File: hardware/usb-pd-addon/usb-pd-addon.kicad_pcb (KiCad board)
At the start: 4 copper layers, 48 x 40 mm, 75 parts, among them J1 Conn_02x10_Odd_Even, J11 Conn_02x02, J2 Conn_02x10_Odd_Even, J3 USB_TYPE_C, J4 USB_TYPE_C, J6 TPAS, J7 TPBS, J8 Conn_02x03_Odd_Even, J9 Conn_02x02, U1 FUSB302B, U10 NC7SB3157P6X, U11 NC7SB3157P6X, U2 AP2171W, U3 SN74AVC1T45DCKR, U4 SN74AVC1T45DCKR, U5 SN74AVC1T45DCKR, U6 SN74AVC1T45DBVR, U7 AP2127K-ADJ, U8 NC7SB3157P6X, U9 NC7SB3157P6X

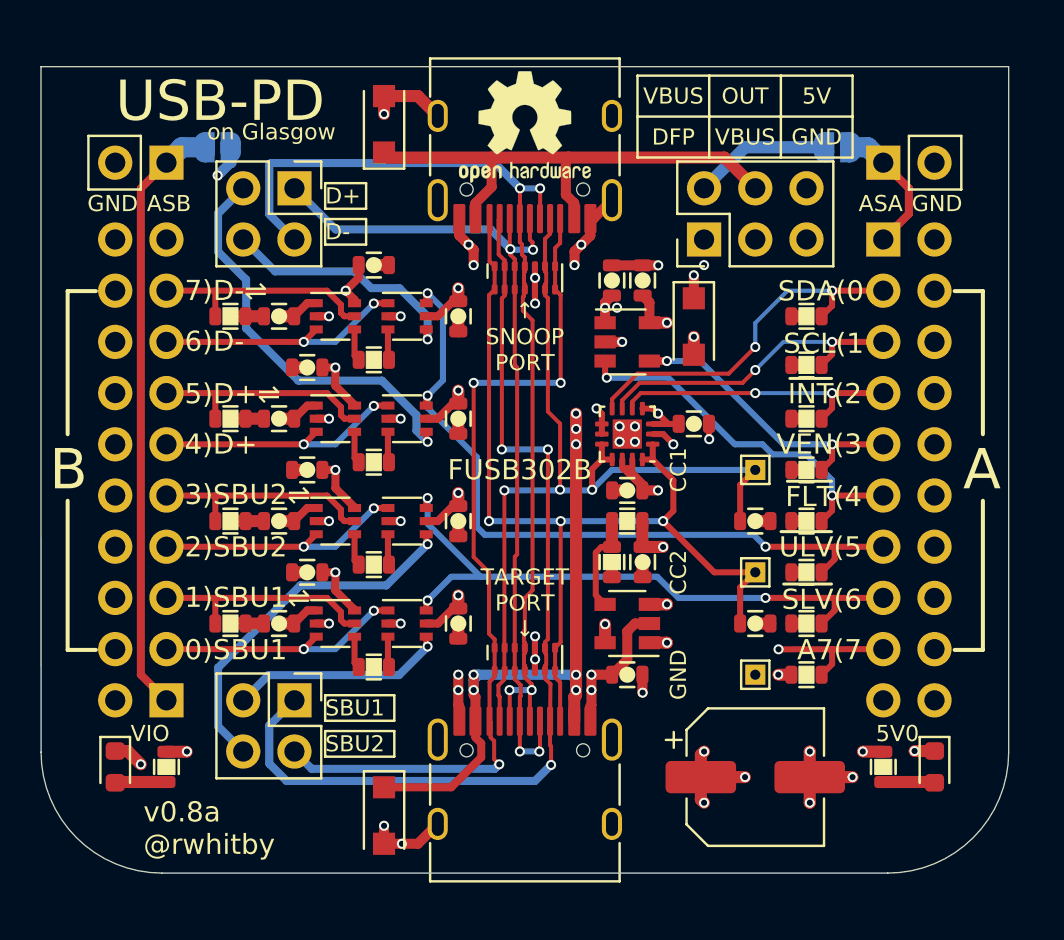
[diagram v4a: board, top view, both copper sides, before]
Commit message: Small silk improvements
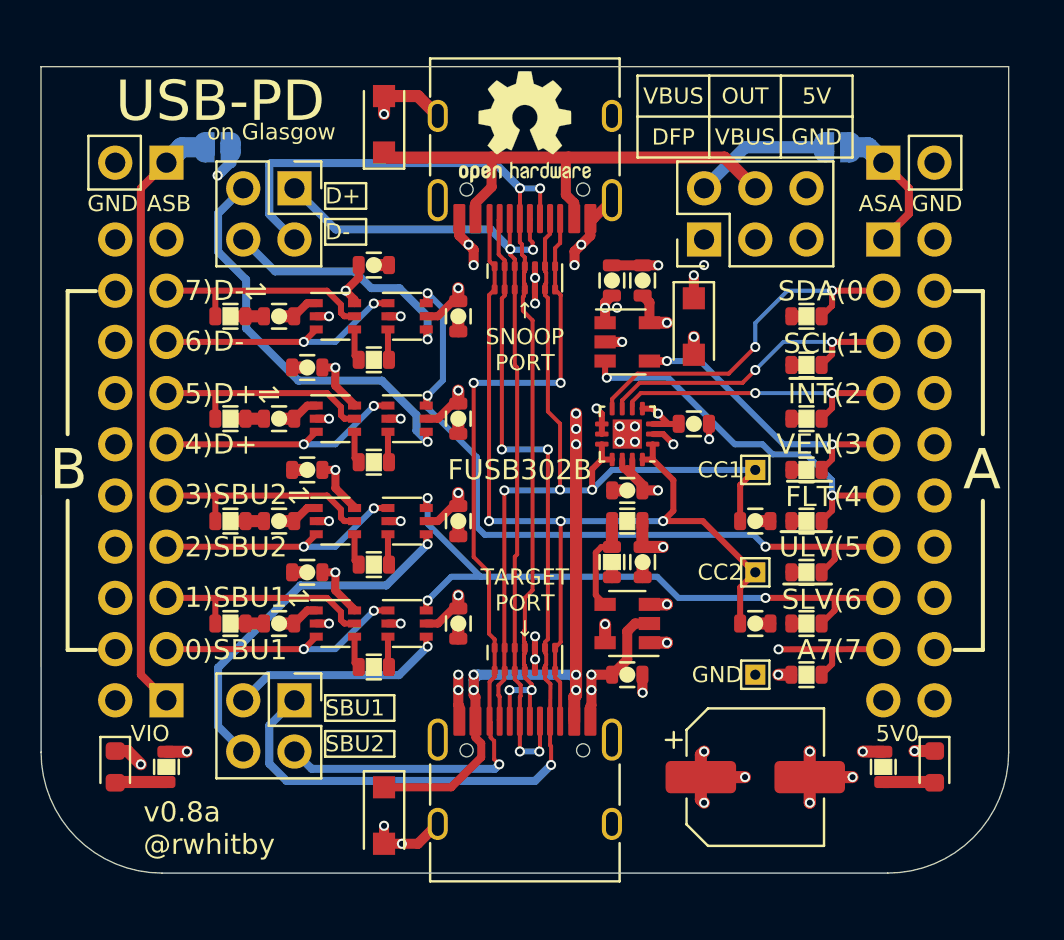
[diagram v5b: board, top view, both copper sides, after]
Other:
- board text added: "⇌D+(5"
- board text added: "⇌D-(7"
- board text added: "⇌SBU1(1"
- board text added: "⇌SBU2(3"
- board text removed: "D+⇌(5"
- board text removed: "D-⇌(7"
- board text removed: "SBU1⇌(1"
- board text removed: "SBU2⇌(3"
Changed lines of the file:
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@@
   )
   (setup
-    (last_trace_width 1)
+    (last_trace_width 0.2)
     (user_trace_width 0.3)
     (user_trace_width 0.4)
@@
       (effects (font (size 1 1) (thickness 0.15)))
     )
-    (fp_text user %R (at 1.27 1.27) (layer F.Fab)
-      (effects (font (size 1 1) (thickness 0.15)))
-    )
     (fp_line (start 0 -1.27) (end 3.81 -1.27) (layer F.Fab) (width 0.1))
     (fp_line (start 3.81 -1.27) (end 3.81 3.81) (layer F.Fab) (width 0.1))
@@
     (fp_line (start 4.35 4.35) (end 4.35 -1.8) (layer F.CrtYd) (width 0.05))
     (fp_line (start 4.35 -1.8) (end -1.8 -1.8) (layer F.CrtYd) (width 0.05))
+    (fp_text user %R (at 1.27 1.27) (layer F.Fab)
+      (effects (font (size 1 1) (thickness 0.15)))
+    )
     (pad 4 thru_hole oval (at 2.54 2.54 270) (size 1.7 1.7) (drill 1) (layers *.Cu *.Mask)
       (net 50 "Net-(J11-Pad4)"))
@@
       (effects (font (size 1 1) (thickness 0.15)))
     )
-    (fp_text user %R (at 1.27 1.27) (layer F.Fab)
-      (effects (font (size 1 1) (thickness 0.15)))
-    )
     (fp_line (start 0 -1.27) (end 3.81 -1.27) (layer F.Fab) (width 0.1))
     (fp_line (start 3.81 -1.27) (end 3.81 3.81) (layer F.Fab) (width 0.1))
@@
     (fp_line (start 4.35 4.35) (end 4.35 -1.8) (layer F.CrtYd) (width 0.05))
     (fp_line (start 4.35 -1.8) (end -1.8 -1.8) (layer F.CrtYd) (width 0.05))
+    (fp_text user %R (at 1.27 1.27) (layer F.Fab)
+      (effects (font (size 1 1) (thickness 0.15)))
+    )
     (pad 4 thru_hole oval (at 2.54 2.54 270) (size 1.7 1.7) (drill 1) (layers *.Cu *.Mask)
       (net 48 "Net-(J9-Pad4)"))
@@
   )
   (gr_poly (pts (xy 61.595 50.90795) (xy 60.325 50.90795) (xy 60.325 49.67605) (xy 61.595 49.67605)) (layer B.Mask) (width 0.1))
-  (gr_text GND (at 63.5 62.23 90) (layer F.SilkS)
-    (effects (font (size 0.8 0.8) (thickness 0.15)))
+  (gr_text GND (at 66.675 62.23) (layer F.SilkS)
+    (effects (font (size 0.8 0.8) (thickness 0.15)) (justify right))
   )
-  (gr_text CC1 (at 63.5 52.07 90) (layer F.SilkS)
-    (effects (font (size 0.8 0.8) (thickness 0.15)))
+  (gr_text CC1 (at 66.675 52.07) (layer F.SilkS)
+    (effects (font (size 0.8 0.8) (thickness 0.15)) (justify right))
   )
-  (gr_text CC2 (at 63.5 57.15 90) (layer F.SilkS)
-    (effects (font (size 0.8 0.8) (thickness 0.15)))
+  (gr_text CC2 (at 66.675 57.15) (layer F.SilkS)
+    (effects (font (size 0.8 0.8) (thickness 0.15)) (justify right))
   )
   (gr_text JLCJLCJLCJLC (at 55.88 71.3105) (layer B.SilkS)
     (effects (font (size 0.8 0.8) (thickness 0.15)) (justify mirror))
   )
-  (gr_text "D-⇌(7" (at 39.5 43.25) (layer B.SilkS)
+  (gr_text "⇌D-(7" (at 39.5 43.25) (layer B.SilkS)
     (effects (font (size 1 1) (thickness 0.15)) (justify right mirror))
   )
@@
     (effects (font (size 1 1) (thickness 0.15)) (justify right mirror))
   )
-  (gr_text "SBU1⇌(1" (at 39.45 58.4) (layer B.SilkS)
+  (gr_text "⇌SBU1(1" (at 39.45 58.4) (layer B.SilkS)
     (effects (font (size 1 1) (thickness 0.15)) (justify right mirror))
   )
@@
     (effects (font (size 1 1) (thickness 0.15)) (justify right mirror))
   )
-  (gr_text "SBU2⇌(3" (at 39.45 53.3) (layer B.SilkS)
+  (gr_text "⇌SBU2(3" (at 39.45 53.3) (layer B.SilkS)
     (effects (font (size 1 1) (thickness 0.15)) (justify right mirror))
   )
@@
     (effects (font (size 1 1) (thickness 0.15)) (justify right mirror))
   )
-  (gr_text "D+⇌(5" (at 39.45 48.3) (layer B.SilkS)
+  (gr_text "⇌D+(5" (at 39.45 48.3) (layer B.SilkS)
     (effects (font (size 1 1) (thickness 0.15)) (justify right mirror))
   )
@@
   (via (at 49.7205 59.69) (size 0.5) (drill 0.3) (layers F.Cu B.Cu) (net 1))
   (segment (start 49.088 59.69) (end 49.7205 59.69) (width 0.4) (layer F.Cu) (net 1) (status 10))
-  (via (at 44.912 60.96) (size 0.5) (drill 0.3) (layers F.Cu B.Cu) (net 17))
   (segment (start 45.532 59.69) (end 46.1645 59.69) (width 0.4) (layer F.Cu) (net 1) (status 10))
   (via (at 46.1645 59.69) (size 0.5) (drill 0.3) (layers F.Cu B.Cu) (net 1))
@@
   (segment (start 62.2225 50.792) (end 62.2225 51.5545) (width 0.3) (layer F.Cu) (net 7) (status 10))
   (segment (start 61.71 51.5545) (end 62.2225 51.5545) (width 0.3) (layer F.Cu) (net 7) (status 10))
-  (segment (start 65.278 57.15) (end 67.31 57.15) (width 0.3) (layer F.Cu) (net 7))
-  (segment (start 62.738 54.61) (end 65.278 57.15) (width 0.3) (layer F.Cu) (net 7))
   (segment (start 66.56 57.9) (end 66.56 59.69) (width 0.3) (layer F.Cu) (net 7))
   (segment (start 67.31 57.15) (end 66.56 57.9) (width 0.3) (layer F.Cu) (net 7))
+  (segment (start 67.2465 57.15) (end 67.31 57.15) (width 0.3) (layer F.Cu) (net 7))
+  (segment (start 64.7065 54.61) (end 67.2465 57.15) (width 0.3) (layer F.Cu) (net 7))
+  (segment (start 62.738 54.61) (end 64.7065 54.61) (width 0.3) (layer F.Cu) (net 7))
   (segment (start 54.63 64.535) (end 54.58001 64.48501) (width 0.2) (layer F.Cu) (net 8) (status 30))
   (segment (start 57.13 40.360346) (end 57.13 39.605) (width 0.2) (layer F.Cu) (net 8) (status 20))
@@
   (segment (start 62.2225 50.292) (end 62.738 50.292) (width 0.3) (layer F.Cu) (net 11) (status 10))
   (segment (start 62.738 50.292) (end 63.246 50.8) (width 0.3) (layer F.Cu) (net 11))
-  (segment (start 67.31 40.386) (end 67.31 40.64) (width 0.5) (layer B.Cu) (net 11) (status 30))
-  (segment (start 65.024 38.1) (end 67.31 40.386) (width 0.6) (layer In2.Cu) (net 11) (status 30))
-  (segment (start 64.77 38.1) (end 65.024 38.1) (width 0.5) (layer B.Cu) (net 11) (status 30))
   (segment (start 53.34 62.992) (end 53.34 62.23) (width 0.5) (layer F.Cu) (net 11))
   (segment (start 53.34 62.484) (end 53.594 62.23) (width 0.5) (layer B.Cu) (net 11))
@@
   (segment (start 53.43 65.346998) (end 53.715001 65.631999) (width 0.4) (layer F.Cu) (net 11))
   (segment (start 53.43 64.535) (end 53.43 65.346998) (width 0.4) (layer F.Cu) (net 11))
+  (segment (start 67.31 40.399998) (end 67.31 40.64) (width 0.8) (layer In2.Cu) (net 11))
+  (segment (start 65.010002 38.1) (end 67.31 40.399998) (width 0.8) (layer In2.Cu) (net 11))
+  (segment (start 64.77 38.1) (end 65.010002 38.1) (width 0.8) (layer In2.Cu) (net 11))
   (segment (start 57.38 41.0652) (end 57.63 40.8152) (width 0.2) (layer F.Cu) (net 12))
   (segment (start 57.38 41.97) (end 57.38 41.0652) (width 0.2) (layer F.Cu) (net 12) (status 10))
@@
   (segment (start 52.578 53.213) (end 53.328001 52.462999) (width 0.6) (layer In2.Cu) (net 14))
   (via (at 69.723 44.45) (size 0.5) (drill 0.3) (layers F.Cu B.Cu) (net 14))
-  (segment (start 63.847998 44.77) (end 64.167998 44.45) (width 0.6) (layer In2.Cu) (net 14))
-  (segment (start 62.926 44.77) (end 63.847998 44.77) (width 0.6) (layer In2.Cu) (net 14))
   (segment (start 78.105 65.452001) (end 78.105 42.545) (width 1) (layer In2.Cu) (net 14))
   (segment (start 78.105 42.545) (end 76.2 40.64) (width 1) (layer In2.Cu) (net 14) (status 20))
@@
   (segment (start 69.723 43.170998) (end 71.390999 41.502999) (width 1) (layer In2.Cu) (net 14))
   (segment (start 69.723 44.45) (end 69.723 43.170998) (width 1) (layer In2.Cu) (net 14))
-  (segment (start 69.723 44.45) (end 64.167998 44.45) (width 1) (layer In2.Cu) (net 14))
   (segment (start 69.723 44.45) (end 69.723 46.863) (width 1) (layer In2.Cu) (net 14))
   (segment (start 62.737954 49.53) (end 62.483954 49.276) (width 1) (layer In2.Cu) (net 14))
@@
   (segment (start 62.733963 53.335999) (end 68.448999 53.335999) (width 1) (layer In2.Cu) (net 14))
   (segment (start 62.483964 53.086) (end 62.733963 53.335999) (width 1) (layer In2.Cu) (net 14))
+  (segment (start 63.246 44.45) (end 62.926 44.77) (width 1) (layer In2.Cu) (net 14))
+  (segment (start 69.723 44.45) (end 63.246 44.45) (width 1) (layer In2.Cu) (net 14))
   (via (at 39.116 66.04) (size 0.5) (drill 0.3) (layers F.Cu B.Cu) (net 15))
   (segment (start 39.104 66.052) (end 39.116 66.04) (width 0.5) (layer F.Cu) (net 15))
@@
   (segment (start 46.482 55.88) (end 48.387 53.975) (width 0.3) (layer B.Cu) (net 16))
   (segment (start 44.912 55.88) (end 46.482 55.88) (width 0.3) (layer B.Cu) (net 16))
+  (via (at 44.912 60.96) (size 0.5) (drill 0.3) (layers F.Cu B.Cu) (net 17))
   (segment (start 44.912 60.96) (end 45.532 60.34) (width 0.3) (layer F.Cu) (net 17) (status 20))
   (segment (start 38.1 60.96) (end 44.912 60.96) (width 0.3) (layer F.Cu) (net 17) (status 10))
@@
   (via (at 64.77 41.91) (size 0.5) (drill 0.3) (layers F.Cu B.Cu) (net 37))
   (segment (start 64.77 40.758016) (end 64.77 40.64) (width 0.6) (layer In2.Cu) (net 37) (status 30))
-  (segment (start 62.903999 43.776001) (end 64.262 42.418) (width 0.6) (layer In2.Cu) (net 37))
-  (segment (start 60.701999 43.776001) (end 62.903999 43.776001) (width 0.6) (layer In2.Cu) (net 37))
-  (segment (start 60.452 44.026) (end 60.701999 43.776001) (width 0.6) (layer In2.Cu) (net 37))
+  (segment (start 63.5 43.18) (end 64.262 42.418) (width 0.6) (layer In2.Cu) (net 37))
+  (segment (start 61.298 43.18) (end 63.5 43.18) (width 0.6) (layer In2.Cu) (net 37))
+  (segment (start 60.452 44.026) (end 61.298 43.18) (width 0.6) (layer In2.Cu) (net 37))
   (segment (start 63.499002 58.42) (end 62.448003 57.369001) (width 0.3) (layer B.Cu) (net 38))
   (segment (start 67.818 58.42) (end 63.499002 58.42) (width 0.3) (layer B.Cu) (net 38))

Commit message: v0.8b: Lots of silk improvements on front side. Relayout of center column of wires. Extended USB-C connectors past board edge.
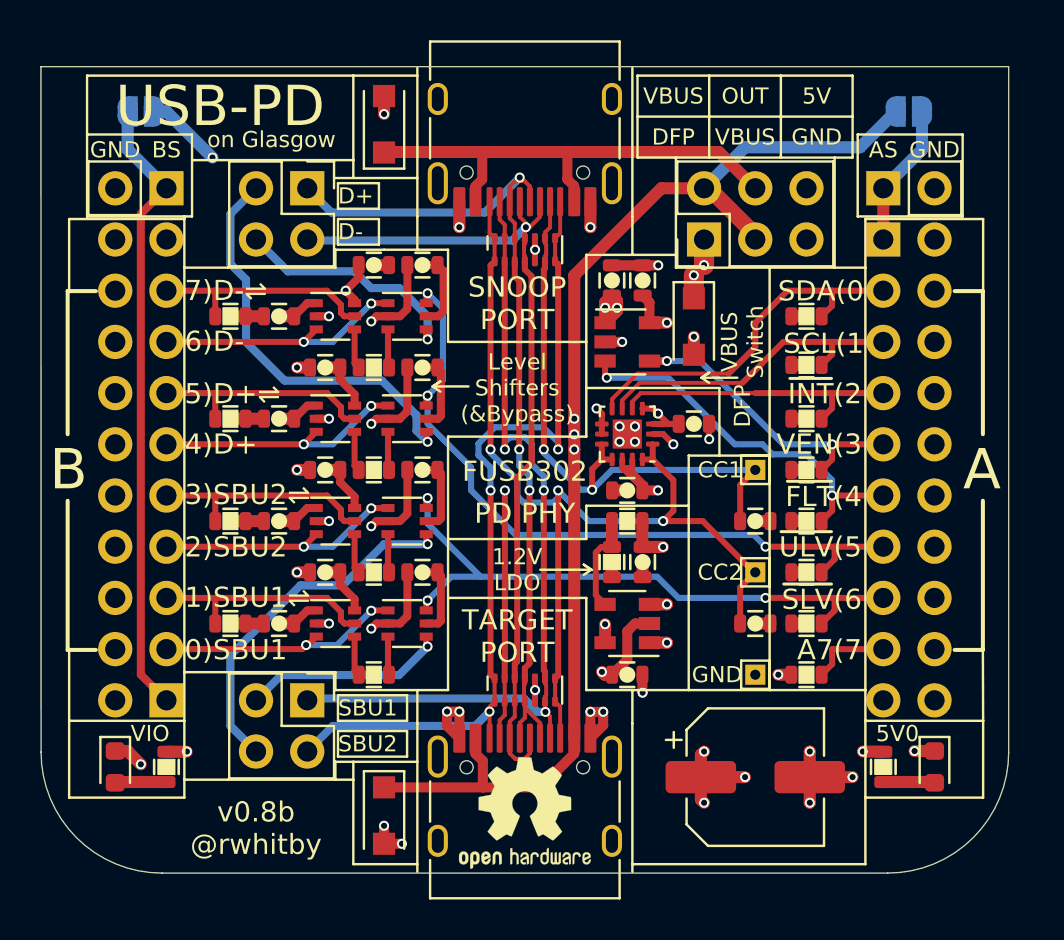
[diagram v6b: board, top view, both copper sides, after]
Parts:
- J11: value Conn_02x02 -> SBU1/SBU2 ISOLATION
- J3: value USB_TYPE_C -> TARGET
- J4: value USB_TYPE_C -> SNOOP
- J6: value TPAS -> ADCA
- J7: value TPBS -> ADCB
- J9: value Conn_02x02 -> D+/D- ISOLATION
- JP1: value Jumper_2_Open -> ADCA-VBUS
- JP2: value Jumper_2_Open -> ADCB-1V2
- R4: value 1K -> 100K
- moved LOGO1 34.0 mm to (55.9, 69.1)
- moved LOGO2 32.8 mm to (55.9, 67.8)
- moved JP2 4.20 mm to (36.8, 34.3)
- moved JP1 3.98 mm to (74.9, 34.3)
- moved C18 3.10 mm to (50.8, 41.9), turned to 180 degrees
- moved C19 3.10 mm to (50.8, 47.0), turned to 180 degrees
- moved C20 3.10 mm to (50.8, 52.1), turned to 180 degrees
- moved C21 3.10 mm to (50.8, 57.1), turned to 180 degrees
- moved D4 1.52 mm to (55.9, 63.0)
- moved D5 1.40 mm to (55.9, 41.1)
- moved J6 1.27 mm to (73.7, 38.1)
- moved J7 1.27 mm to (38.1, 38.1)
- moved C11 0.89 mm to (46.0, 47.0)
- moved C12 0.89 mm to (46.0, 57.1)
- moved C4 0.89 mm to (46.0, 52.1)
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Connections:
- net /ADJ_USB renamed Net-(R10-Pad2)
- net /~SBU_1V2 renamed /~SLV
- net /~USB_1V2 renamed /~ULV
- D4 pad 11: /USBN -> /USBP
- D4 pad 12: /USBP -> /USBN
- D4 pad 3: /USBP -> /USBN
- D4 pad 4: /USBN -> /USBP
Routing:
- net +5V: track 160.6 -> 169.6 mm
- net /SBU1: track 48.3 -> 41.5 mm
- net /USBN: track 49.6 -> 42.9 mm, vias 4 -> 1
- net /VBUS: track 72.3 -> 67.6 mm, vias 8 -> 4
- net /1.2V: track 62.9 -> 66.3 mm
- net GND: track 209.9 -> 213.0 mm, vias 57 -> 50
- net /A7: track 6.68 -> 4.02 mm, vias 1 -> 0
- net /CC2: track 47.4 -> 49.9 mm
- net /CC1: track 44.3 -> 46.1 mm
- net /VBUS_DFP: track 9.80 -> 11.5 mm
- net /VBUS_OUT: track 25.8 -> 24.4 mm
- net /BS: track 29.9 -> 31.1 mm
- net /~ULV: track 36.4 -> 35.5 mm
- net /SBU2: track 43.1 -> 42.3 mm
- net Net-(J9-Pad4): track 12.4 -> 11.8 mm
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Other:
- board text added: "1.2V LDO"
- board text added: "AS"
- board text added: "BS"
- board text added: "CC-BY-SA"
- board text added: "FUSB302"
- board text added: "Level Shifters (&Bypass)"
- board text added: "PD PHY"
- board text added: "SNOOP PORT"
- board text added: "TARGET PORT"
- board text added: "VBUS Switch"
- board text added: "v0.8b @rwhitby"
- board text removed: "ASA"
- board text removed: "ASB"
- board text removed: "Glasgow USB-PD @rwhitby"
- board text removed: "TARGET PORT ↓"
- board text removed: "v0.8a @rwhitby"
- board text removed: "v0.8a CC-BY-SA"
- board text removed: "↑ SNOOP PORT"

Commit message: Ordered annotations and rotated components.
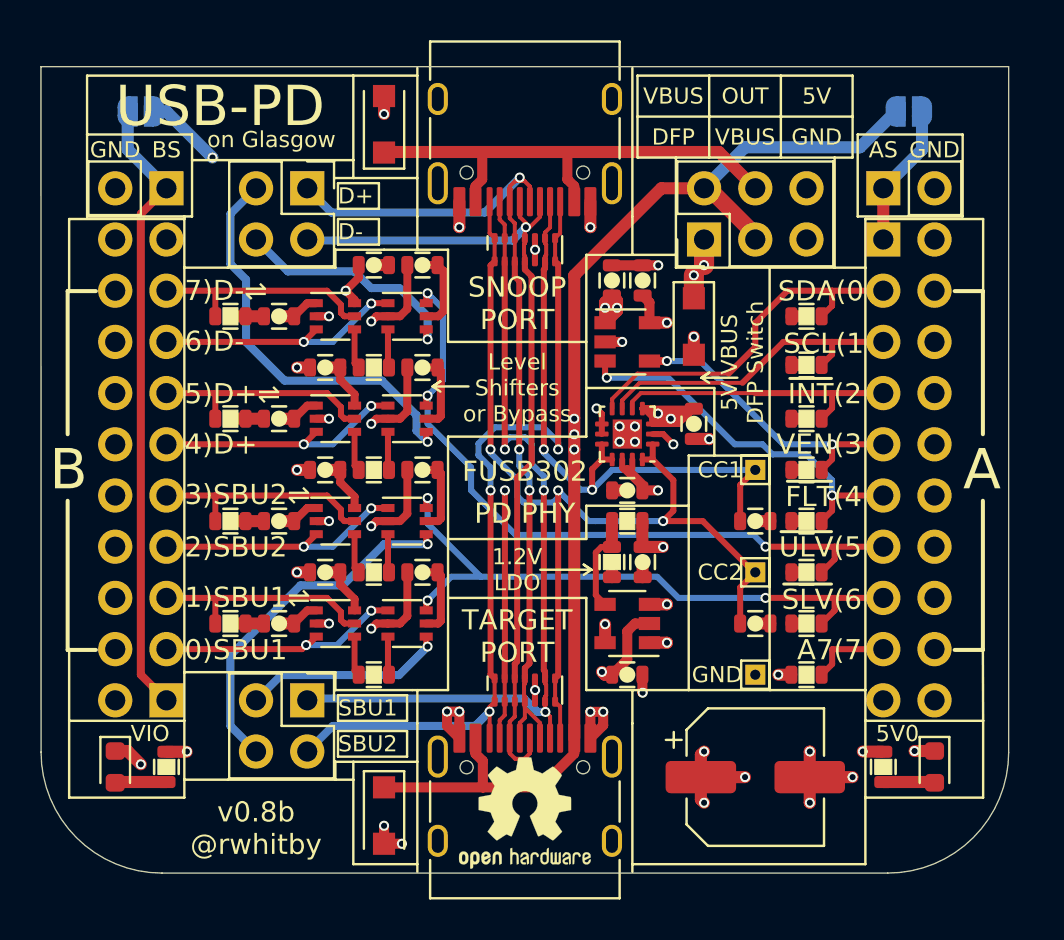
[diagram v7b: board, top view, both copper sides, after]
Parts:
- removed the C8 at (64.3, 49.8)
- added C15: 0.1u, pkl_dipol:C_0603, F.Cu at (64.3, 49.8)
- U7: renamed from U6; value SN74AVC1T45DBVR -> SN74AVC1T45DCKR
- turned C10 to 0 degrees
- turned C11 to 0 degrees
- turned C14 to 90 degrees
- turned C17 to 90 degrees
- turned C19 to 0 degrees
- turned C2 to 0 degrees
- turned C20 to 0 degrees
- turned C4 to 0 degrees
- turned C5 to 0 degrees
- turned C7 to 0 degrees
- turned C8 to 0 degrees
- turned R11 to 0 degrees
- turned R13 to 0 degrees
- turned R15 to 0 degrees
- turned R17 to 0 degrees
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- renumbered C3 to C1, C12 to C10, C21 to C11, C10 to C12, C14 to C13, C13 to C14, C6 to C16, C7 to C17, C5 to C18, C15 to C19, C18 to C2, C17 to C20, C16 to C21, C1 to C3, C11 to C4, C19 to C5, C9 to C6, C4 to C7, C20 to C8, C2 to C9, J3 to J1, J4 to J2, J1 to J3, J2 to J4, J7 to J5, J9 to J7, J11 to J8, J8 to J9, R17 to R11, R11 to R12, R19 to R13, R13 to R14, R18 to R15, R12 to R16, R20 to R17, R14 to R18, R15 to R19, R16 to R20, U3 to U1, U1 to U10, U7 to U11, U8 to U2, U5 to U3, U9 to U4, U4 to U5, U10 to U6, U11 to U8, U2 to U9
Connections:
- C10 pad 1: /1.2V -> GND
- C10 pad 2: GND -> /1.2V
- C11 pad 1: +5V -> GND
- C11 pad 2: GND -> +5V
- C14 pad 1: GND -> +5V
- C14 pad 2: +5V -> GND
- C17 pad 1: /1.2V -> GND
- C17 pad 2: GND -> /1.2V
- C19 pad 1: GND -> /CC1
- C19 pad 2: /CC1 -> GND
- C2 pad 1: +5V -> GND
- C2 pad 2: GND -> +5V
- C20 pad 1: GND -> /CC2
- C20 pad 2: /CC2 -> GND
- C4 pad 1: /1.2V -> GND
- C4 pad 2: GND -> /1.2V
- C5 pad 1: +5V -> GND
- C5 pad 2: GND -> +5V
- C7 pad 1: /1.2V -> GND
- C7 pad 2: GND -> /1.2V
- C8 pad 1: +5V -> GND
- C8 pad 2: GND -> +5V
- R11 pad 1: GND -> /USBN_DIR
- R11 pad 2: /USBN_DIR -> GND
- R13 pad 1: GND -> /USBP_DIR
- R13 pad 2: /USBP_DIR -> GND
- R15 pad 1: GND -> /SBU2_DIR
- R15 pad 2: /SBU2_DIR -> GND
- R17 pad 1: GND -> /SBU1_DIR
- R17 pad 2: /SBU1_DIR -> GND
- R5 pad 1: /~FLT -> +5V
- R5 pad 2: +5V -> /~FLT
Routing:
- net +5V: track 169.6 -> 180.5 mm, vias 15 -> 16
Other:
- board text added: "5V VBUS DFP Switch"
- board text added: "Level Shifters or Bypass"
- board text removed: "Level Shifters (&Bypass)"
- board text removed: "VBUS Switch"
